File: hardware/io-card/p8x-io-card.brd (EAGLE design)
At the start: 160 x 100 mm, 56 parts, among them J1 FABC96R, J2 SERIAL, J3 RTC 3-WIRE, SW1 INPUT, U1 IO PAGE, U10 LED PORT, U11 MON A-LO, U12 MON A-HI, U13 MON D, U14 ACIA, U15 74HCT00, U16 RTC DNP, U2 PORT DEC, U3 DOE DEC, U4 DLD DEC, U5 74HCT32, U6 74HCT08, U7 BAUD DIV, U8 RS232, U9 SW IN, X2 2.4576MHZ, X3 32.768KHZ

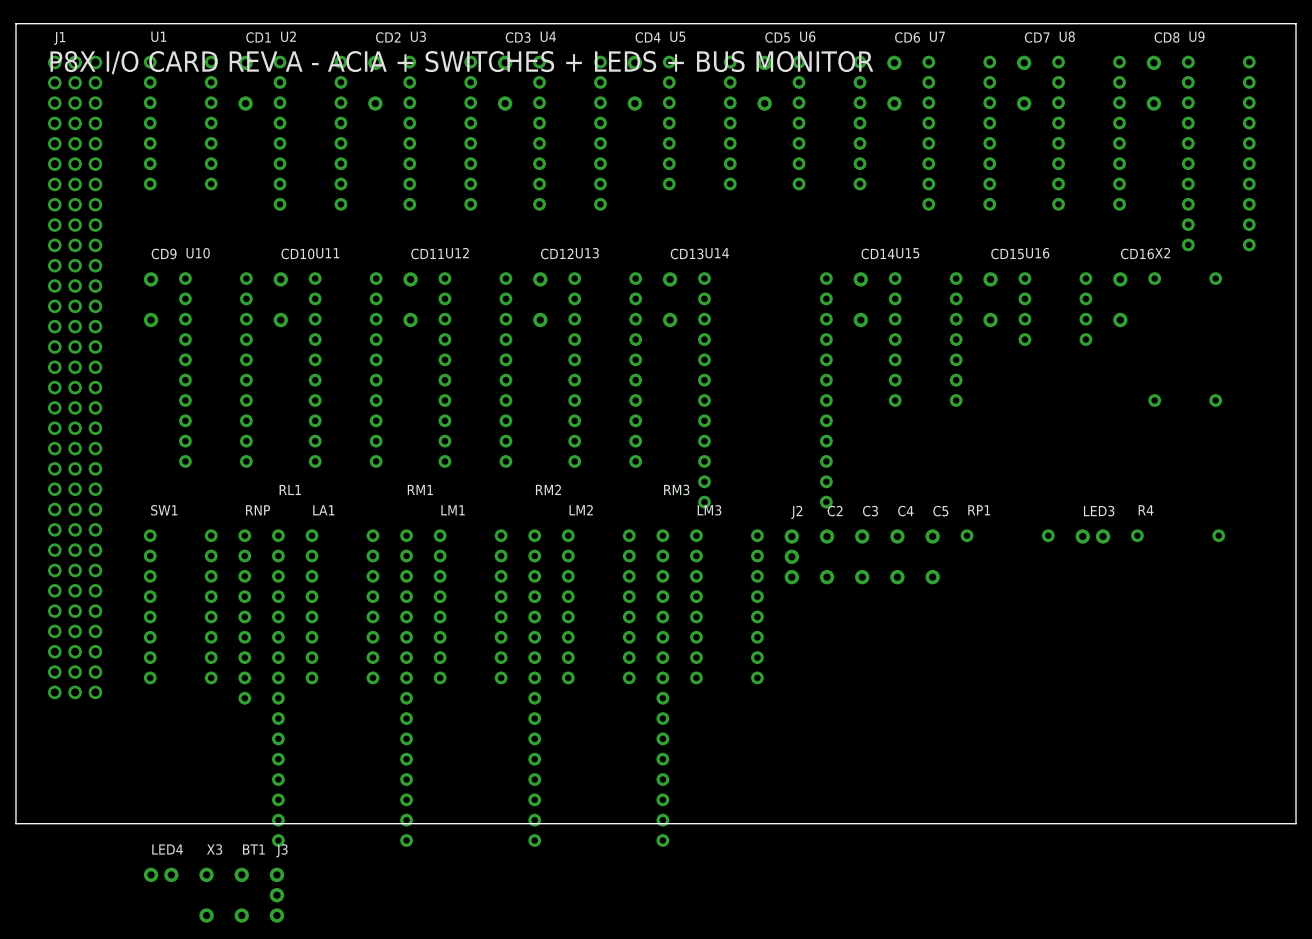
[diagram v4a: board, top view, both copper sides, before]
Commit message: feat(hw): card DIN connector mounting holes (DIN96C, standard DIN 41612)
The card edge connector (FABC96R) needs board mounting holes; the footprint had
only the 96 signal pins. Split the connector into two packages so cards and the
backplane don't share holes:
- DIN96C (card): 96 pins + 2 mounting holes on the centreline (x=2.54), 94.0mm
  apart, drill 2.8mm for M2.5. Emitted as non-plated <hole> elements (new
  lib_xml branch for MH* entries). DEV["DIN96C"] = DIN96 pins, pkg DIN96C.
- DIN96 (backplane receptacle): pins only, unchanged.
Card J1 (all 6: 5 plug-in via card() + memory) now uses DIN96C; backplane slots
keep DIN96. Fixed card() to honor the J1 package on the board side and in CARDS
(was hardcoding "DIN96", which both dropped the holes and mislabeled the BOM).

Verified: each card .brd has 2 holes, backplane 0; overlap guard clean (the
shared-package version collided with backplane terminators); BOM shows 6 card
(DIN96C) + 10 backplane. All boards 0 errors, all 6 suites pass.

VERIFY the 94mm spacing / 2.8mm dia against the FABC96R datasheet.

Co-Authored-By: Claude Opus 4.8 <noreply@anthropic.com>
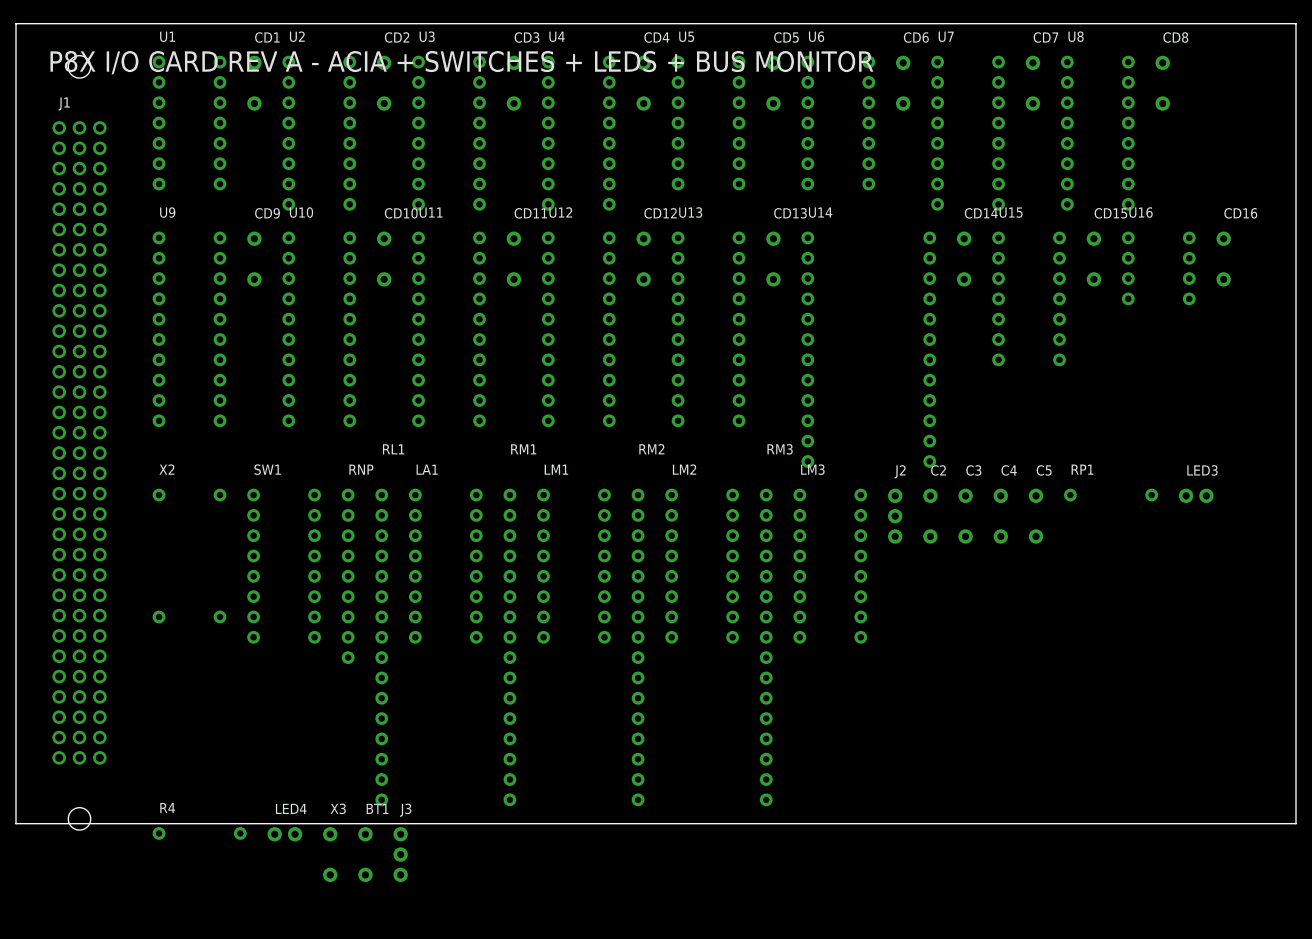
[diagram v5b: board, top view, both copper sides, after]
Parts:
- J1: device p8x:DIN96 -> p8x:DIN96C
- moved U9 130.5 mm to (17.9, 73.2)
- moved R4 127.8 mm to (17.9, -1.22)
- moved X2 127.4 mm to (17.9, 41.1)
- moved LED4 16.3 mm to (32.3, -1.32)
- moved BT1 16.3 mm to (43.7, -1.32)
- moved J3 16.3 mm to (48.1, -1.32)
- moved X3 16.3 mm to (39.3, -1.32)
- moved CD15 13.9 mm to (134.7, 73.1)
- moved CD16 13.9 mm to (151.0, 73.1)
- moved RP1 13.9 mm to (131.8, 41.1)
- moved U12 13.9 mm to (66.5, 73.2)
- moved C2 13.9 mm to (114.3, 41.0)
- moved C3 13.9 mm to (118.7, 41.0)
- moved C5 13.9 mm to (127.5, 41.0)
- moved CD10 13.9 mm to (46.0, 73.1)
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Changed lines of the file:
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@@
 <designrules name="default"><param name="layerSetup" value="(1*2*15*16)"/></designrules>
 <elements>
-<element name="J1" library="p8x" package="DIN96" value="FABC96R" x="4.85" y="95.15"/>
-<element name="U1" library="p8x" package="DIP14" value="IO PAGE" x="16.78" y="95.20"/>
-<element name="CD1" library="p8x" package="C_DISC" value="100N" x="28.70" y="95.10"/>
-<element name="U2" library="p8x" package="DIP16" value="PORT DEC" x="33.00" y="95.20"/>
-<element name="CD2" library="p8x" package="C_DISC" value="100N" x="44.92" y="95.10"/>
-<element name="U3" library="p8x" package="DIP16" value="DOE DEC" x="49.22" y="95.20"/>
-<element name="CD3" library="p8x" package="C_DISC" value="100N" x="61.14" y="95.10"/>
-<element name="U4" library="p8x" package="DIP16" value="DLD DEC" x="65.44" y="95.20"/>
-<element name="CD4" library="p8x" package="C_DISC" value="100N" x="77.36" y="95.10"/>
-<element name="U5" library="p8x" package="DIP14" value="74HCT32" x="81.66" y="95.20"/>
-<element name="CD5" library="p8x" package="C_DISC" value="100N" x="93.58" y="95.10"/>
-<element name="U6" library="p8x" package="DIP14" value="74HCT08" x="97.88" y="95.20"/>
-<element name="CD6" library="p8x" package="C_DISC" value="100N" x="109.80" y="95.10"/>
-<element name="U7" library="p8x" package="DIP16" value="BAUD DIV" x="114.10" y="95.20"/>
-<element name="CD7" library="p8x" package="C_DISC" value="100N" x="126.02" y="95.10"/>
-<element name="U8" library="p8x" package="DIP16" value="RS232" x="130.32" y="95.20"/>
-<element name="CD8" library="p8x" package="C_DISC" value="100N" x="142.24" y="95.10"/>
-<element name="U9" library="p8x" package="DIP20" value="SW IN" x="146.54" y="95.20"/>
-<element name="CD9" library="p8x" package="C_DISC" value="100N" x="16.88" y="68.04"/>
-<element name="U10" library="p8x" package="DIP20" value="LED PORT" x="21.18" y="68.14"/>
-<element name="CD10" library="p8x" package="C_DISC" value="100N" x="33.10" y="68.04"/>
-<element name="U11" library="p8x" package="DIP20" value="MON A-LO" x="37.40" y="68.14"/>
-<element name="CD11" library="p8x" package="C_DISC" value="100N" x="49.32" y="68.04"/>
-<element name="U12" library="p8x" package="DIP20" value="MON A-HI" x="53.62" y="68.14"/>
-<element name="CD12" library="p8x" package="C_DISC" value="100N" x="65.54" y="68.04"/>
-<element name="U13" library="p8x" package="DIP20" value="MON D" x="69.84" y="68.14"/>
-<element name="CD13" library="p8x" package="C_DISC" value="100N" x="81.76" y="68.04"/>
-<element name="U14" library="p8x" package="DIP24W" value="ACIA" x="86.06" y="68.14"/>
-<element name="CD14" library="p8x" package="C_DISC" value="100N" x="105.60" y="68.04"/>
-<element name="U15" library="p8x" package="DIP14" value="74HCT00" x="109.90" y="68.14"/>
-<element name="CD15" library="p8x" package="C_DISC" value="100N" x="121.82" y="68.04"/>
-<element name="U16" library="p8x" package="DIP8" value="RTC DNP" x="126.12" y="68.14"/>
-<element name="CD16" library="p8x" package="C_DISC" value="100N" x="138.04" y="68.04"/>
-<element name="X2" library="p8x" package="OSC4" value="2.4576MHZ" x="142.34" y="68.14"/>
-<element name="SW1" library="p8x" package="DIP16" value="INPUT" x="16.78" y="36.00"/>
-<element name="RNP" library="p8x" package="SIP9" value="8X10K" x="28.60" y="36.00"/>
-<element name="RL1" library="p8x" package="SIP16" value="8X330R" x="32.80" y="38.54"/>
-<element name="LA1" library="p8x" package="DIP16" value="PORT LEDS" x="37.00" y="36.00"/>
-<element name="RM1" library="p8x" package="SIP16" value="8X330R" x="48.82" y="38.54"/>
-<element name="LM1" library="p8x" package="DIP16" value="A0-7" x="53.02" y="36.00"/>
-<element name="RM2" library="p8x" package="SIP16" value="8X330R" x="64.84" y="38.54"/>
-<element name="LM2" library="p8x" package="DIP16" value="A8-15" x="69.04" y="36.00"/>
-<element name="RM3" library="p8x" package="SIP16" value="8X330R" x="80.86" y="38.54"/>
-<element name="LM3" library="p8x" package="DIP16" value="D0-7" x="85.06" y="36.00"/>
-<element name="J2" library="p8x" package="HDR3" value="SERIAL" x="96.98" y="35.90"/>
-<element name="C2" library="p8x" package="C_DISC" value="1U" x="101.38" y="35.90"/>
-<element name="C3" library="p8x" package="C_DISC" value="1U" x="105.78" y="35.90"/>
-<element name="C4" library="p8x" package="C_DISC" value="1U" x="110.18" y="35.90"/>
-<element name="C5" library="p8x" package="C_DISC" value="1U" x="114.58" y="35.90"/>
-<element name="RP1" library="p8x" package="R_AXIAL" value="1K" x="118.88" y="36.00"/>
-<element name="LED3" library="p8x" package="LED5" value="PWR-GRN" x="133.34" y="35.90"/>
-<element name="R4" library="p8x" package="R_AXIAL" value="1K" x="140.18" y="36.00"/>
-<element name="LED4" library="p8x" package="LED5" value="IOSEL-YEL" x="16.88" y="-6.40"/>
-<element name="X3" library="p8x" package="C_DISC" value="32.768KHZ" x="23.82" y="-6.40"/>
-<element name="BT1" library="p8x" package="CP_RADIAL" value="CR2032" x="28.22" y="-6.40"/>
-<element name="J3" library="p8x" package="HDR3" value="RTC 3-WIRE" x="32.62" y="-6.40"/>
+<element name="J1" library="p8x" package="DIN96C" value="FABC96R" x="5.40" y="86.97"/>
+<element name="U1" library="p8x" package="DIP14" value="IO PAGE" x="17.88" y="95.20"/>
+<element name="CD1" library="p8x" package="C_DISC" value="100N" x="29.80" y="95.10"/>
+<element name="U2" library="p8x" package="DIP16" value="PORT DEC" x="34.10" y="95.20"/>
+<element name="CD2" library="p8x" package="C_DISC" value="100N" x="46.02" y="95.10"/>
+<element name="U3" library="p8x" package="DIP16" value="DOE DEC" x="50.32" y="95.20"/>
+<element name="CD3" library="p8x" package="C_DISC" value="100N" x="62.24" y="95.10"/>
+<element name="U4" library="p8x" package="DIP16" value="DLD DEC" x="66.54" y="95.20"/>
+<element name="CD4" library="p8x" package="C_DISC" value="100N" x="78.46" y="95.10"/>
+<element name="U5" library="p8x" package="DIP14" value="74HCT32" x="82.76" y="95.20"/>
+<element name="CD5" library="p8x" package="C_DISC" value="100N" x="94.68" y="95.10"/>
+<element name="U6" library="p8x" package="DIP14" value="74HCT08" x="98.98" y="95.20"/>
+<element name="CD6" library="p8x" package="C_DISC" value="100N" x="110.90" y="95.10"/>
+<element name="U7" library="p8x" package="DIP16" value="BAUD DIV" x="115.20" y="95.20"/>
+<element name="CD7" library="p8x" package="C_DISC" value="100N" x="127.12" y="95.10"/>
+<element name="U8" library="p8x" package="DIP16" value="RS232" x="131.42" y="95.20"/>
+<element name="CD8" library="p8x" package="C_DISC" value="100N" x="143.34" y="95.10"/>
+<element name="U9" library="p8x" package="DIP20" value="SW IN" x="17.88" y="73.22"/>
+<element name="CD9" library="p8x" package="C_DISC" value="100N" x="29.80" y="73.12"/>
+<element name="U10" library="p8x" package="DIP20" value="LED PORT" x="34.10" y="73.22"/>
+<element name="CD10" library="p8x" package="C_DISC" value="100N" x="46.02" y="73.12"/>
+<element name="U11" library="p8x" package="DIP20" value="MON A-LO" x="50.32" y="73.22"/>
+<element name="CD11" library="p8x" package="C_DISC" value="100N" x="62.24" y="73.12"/>
+<element name="U12" library="p8x" package="DIP20" value="MON A-HI" x="66.54" y="73.22"/>
+<element name="CD12" library="p8x" package="C_DISC" value="100N" x="78.46" y="73.12"/>
+<element name="U13" library="p8x" package="DIP20" value="MON D" x="82.76" y="73.22"/>
+<element name="CD13" library="p8x" package="C_DISC" value="100N" x="94.68" y="73.12"/>
+<element name="U14" library="p8x" package="DIP24W" value="ACIA" x="98.98" y="73.22"/>
+<element name="CD14" library="p8x" package="C_DISC" value="100N" x="118.52" y="73.12"/>
+<element name="U15" library="p8x" package="DIP14" value="74HCT00" x="122.82" y="73.22"/>
+<element name="CD15" library="p8x" package="C_DISC" value="100N" x="134.74" y="73.12"/>
+<element name="U16" library="p8x" package="DIP8" value="RTC DNP" x="139.04" y="73.22"/>
+<element name="CD16" library="p8x" package="C_DISC" value="100N" x="150.96" y="73.12"/>
+<element name="X2" library="p8x" package="OSC4" value="2.4576MHZ" x="17.88" y="41.08"/>
+<element name="SW1" library="p8x" package="DIP16" value="INPUT" x="29.70" y="41.08"/>
+<element name="RNP" library="p8x" package="SIP9" value="8X10K" x="41.52" y="41.08"/>
+<element name="RL1" library="p8x" package="SIP16" value="8X330R" x="45.72" y="43.62"/>
+<element name="LA1" library="p8x" package="DIP16" value="PORT LEDS" x="49.92" y="41.08"/>
+<element name="RM1" library="p8x" package="SIP16" value="8X330R" x="61.74" y="43.62"/>
+<element name="LM1" library="p8x" package="DIP16" value="A0-7" x="65.94" y="41.08"/>
+<element name="RM2" library="p8x" package="SIP16" value="8X330R" x="77.76" y="43.62"/>
+<element name="LM2" library="p8x" package="DIP16" value="A8-15" x="81.96" y="41.08"/>
+<element name="RM3" library="p8x" package="SIP16" value="8X330R" x="93.78" y="43.62"/>
+<element name="LM3" library="p8x" package="DIP16" value="D0-7" x="97.98" y="41.08"/>
+<element name="J2" library="p8x" package="HDR3" value="SERIAL" x="109.90" y="40.98"/>
+<element name="C2" library="p8x" package="C_DISC" value="1U" x="114.30" y="40.98"/>
+<element name="C3" library="p8x" package="C_DISC" value="1U" x="118.70" y="40.98"/>
+<element name="C4" library="p8x" package="C_DISC" value="1U" x="123.10" y="40.98"/>
+<element name="C5" library="p8x" package="C_DISC" value="1U" x="127.50" y="40.98"/>
+<element name="RP1" library="p8x" package="R_AXIAL" value="1K" x="131.80" y="41.08"/>
+<element name="LED3" library="p8x" package="LED5" value="PWR-GRN" x="146.26" y="40.98"/>
+<element name="R4" library="p8x" package="R_AXIAL" value="1K" x="17.88" y="-1.22"/>
+<element name="LED4" library="p8x" package="LED5" value="IOSEL-YEL" x="32.34" y="-1.32"/>
+<element name="X3" library="p8x" package="C_DISC" value="32.768KHZ" x="39.28" y="-1.32"/>
+<element name="BT1" library="p8x" package="CP_RADIAL" value="CR2032" x="43.68" y="-1.32"/>
+<element name="J3" library="p8x" package="HDR3" value="RTC 3-WIRE" x="48.08" y="-1.32"/>
 </elements><signals>
 <signal name="-MEMW">

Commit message: fix(hardware): connect IC power pins on the card()-built boards
Schematic-review fix. card() wired the edge-connector and decoupling-cap pins to
VCC/GND but never added each IC's own VCC/GND supply pin, so on control, regbank,
ALU, I/O, and CF the chips' power pads were not members of the power pours and
would not have been powered. (The hand-built memory card already did this; the
backplane has no ICs. validate() couldn't catch it — it checks pin-name legality,
not connectivity.)

- card(): append (ref,"VCC")/(ref,"GND") for every IC, skipping any pin already
  wired by hand (idempotent — avoids duplicate pinrefs, e.g. ALU U16 GND)
- regenerated all 7 boards (.sch/.brd), 0 validation errors
- board-level audit: every IC on every card now has both VCC and GND on the
  power signals
- BACKLOG: moved the critical item to DONE; theory docs' power-pin callouts
  updated to "fixed"

Co-Authored-By: Claude Opus 4.8 <noreply@anthropic.com>
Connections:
- net GND: now also U1.7, U10.10, U11.10, U12.10, U13.10, U14.1, U15.7, U2.8, U3.8, U4.8, U5.7, U6.7, U7.8, U8.15, U9.10
- net VCC: now also U1.14, U10.20, U11.20, U12.20, U13.20, U14.12, U15.14, U2.16, U3.16, U4.16, U5.14, U6.14, U7.16, U8.16, U9.20
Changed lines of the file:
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@@
 <contactref element="CD15" pad="2"/>
 <contactref element="CD16" pad="2"/>
+<contactref element="U1" pad="7"/>
+<contactref element="U2" pad="8"/>
+<contactref element="U3" pad="8"/>
+<contactref element="U4" pad="8"/>
+<contactref element="U5" pad="7"/>
+<contactref element="U6" pad="7"/>
+<contactref element="U7" pad="8"/>
+<contactref element="U8" pad="15"/>
+<contactref element="U9" pad="10"/>
+<contactref element="U10" pad="10"/>
+<contactref element="U11" pad="10"/>
+<contactref element="U12" pad="10"/>
+<contactref element="U13" pad="10"/>
+<contactref element="U14" pad="1"/>
+<contactref element="U15" pad="7"/>
 <polygon width="0.254" layer="2" isolate="0.3" rank="1">
 <vertex x="0" y="0"/>
@@
 <contactref element="CD15" pad="1"/>
 <contactref element="CD16" pad="1"/>
+<contactref element="U1" pad="14"/>
+<contactref element="U2" pad="16"/>
+<contactref element="U3" pad="16"/>
+<contactref element="U4" pad="16"/>
+<contactref element="U5" pad="14"/>
+<contactref element="U6" pad="14"/>
+<contactref element="U7" pad="16"/>
+<contactref element="U8" pad="16"/>
+<contactref element="U9" pad="20"/>
+<contactref element="U10" pad="20"/>
+<contactref element="U11" pad="20"/>
+<contactref element="U12" pad="20"/>
+<contactref element="U13" pad="20"/>
+<contactref element="U14" pad="12"/>
+<contactref element="U15" pad="14"/>
 <polygon width="0.254" layer="15" isolate="0.3" rank="1">
 <vertex x="0" y="0"/>

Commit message: feat(backplane): row-B even pins become spare bus lines (SPARE12-23)
Row B was a solid ground guard (B3-26 all GND). Per request, B3-26 now ALTERNATE:
odd pins stay GND (still a guard between most signal pairs), and the 12 even pins
(B4,B6,..,B26) become spare bus lines SPARE12-SPARE23, routed slot-to-slot — so
new signals can be added later without re-spinning the backplane. B27-30
(CLRC/BSEL/IRQ/SPARE11) unchanged.

- busnet() updated in all three copies (gen_eagle, gen_bus_pdf, gen_bus_card)
- backplane .brd routes the 12 new spares (mirrors the B27-30 routing); odd-pin
  grounds remain on the GND pour
- every card regenerated: their connectors no longer tie the even B pins to GND
  (those are spare lines now) — they simply don't connect the spares
- all 8 boards validate (0 errors); schematic + bus PDFs regenerated
- docs updated: bus-definition (pin map + notes), backplane theory + design notes
- net signal-integrity trade noted: a solid guard shields slightly better; the
  alternation was chosen deliberately for expansion room

Co-Authored-By: Claude Opus 4.8 <noreply@anthropic.com>
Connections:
- net GND: no longer J1.B10, J1.B12, J1.B14, J1.B16, J1.B18, J1.B20, J1.B22, J1.B24, J1.B26, J1.B4, J1.B6, J1.B8
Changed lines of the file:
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@@
 <contactref element="J1" pad="A32"/>
 <contactref element="J1" pad="B3"/>
-<contactref element="J1" pad="B4"/>
 <contactref element="J1" pad="B5"/>
-<contactref element="J1" pad="B6"/>
 <contactref element="J1" pad="B7"/>
-<contactref element="J1" pad="B8"/>
 <contactref element="J1" pad="B9"/>
-<contactref element="J1" pad="B10"/>
 <contactref element="J1" pad="B11"/>
-<contactref element="J1" pad="B12"/>
 <contactref element="J1" pad="B13"/>
-<contactref element="J1" pad="B14"/>
 <contactref element="J1" pad="B15"/>
-<contactref element="J1" pad="B16"/>
 <contactref element="J1" pad="B17"/>
-<contactref element="J1" pad="B18"/>
 <contactref element="J1" pad="B19"/>
-<contactref element="J1" pad="B20"/>
 <contactref element="J1" pad="B21"/>
-<contactref element="J1" pad="B22"/>
 <contactref element="J1" pad="B23"/>
-<contactref element="J1" pad="B24"/>
 <contactref element="J1" pad="B25"/>
-<contactref element="J1" pad="B26"/>
 <contactref element="J1" pad="B31"/>
 <contactref element="J1" pad="B32"/>
